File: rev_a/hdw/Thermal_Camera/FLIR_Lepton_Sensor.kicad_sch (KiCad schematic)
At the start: 25 parts

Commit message: lots of schematic progress
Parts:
- C?: renamed from C1102; footprint Capacitors_SMD:C_0603 -> (none); Digi-Key PN 1276-1935-1-ND -> (none); display_footprint 0603 -> (none)
- C? (x3): renamed from C1501; footprint Capacitors_SMD:C_0603 -> (none); Digi-Key PN 1276-1935-1-ND -> (none); display_footprint 0603 -> (none)
- C?: renamed from C1104; footprint Capacitors_SMD:C_0603 -> (none); Digi-Key PN 1276-1871-1-ND -> (none); display_footprint 0603 -> (none)
- L?: renamed from L1101; footprint Inductors_SMD:L_0603 -> (none); Digi-Key PN 490-1014-1-ND -> (none)
- R2401: renamed from R?; footprint Resistors_SMD:R_0603 -> (none); Digi-Key PN 541-10.0KHCT-ND -> (none); Wattage 1/10W -> (none); display_footprint 0603 -> (none)
- R2410, R2411, R2412, R2413, R2414: renamed from R?; footprint Resistors_SMD:R_0603 -> (none); Digi-Key PN 541-2982-1-ND -> (none); Wattage 1/10W -> (none); display_footprint 0603 -> (none)
- R?: renamed from R1103; footprint Resistors_SMD:R_0603 -> (none); Digi-Key PN 541-10.0HCT-ND -> (none); Wattage 1/10W -> (none); display_footprint 0603 -> (none)
- R? (x7): renamed from R1501; footprint Resistors_SMD:R_0603 -> (none); Digi-Key PN 541-10.0KHCT-ND -> (none); Wattage 1/10W -> (none); display_footprint 0603 -> (none)
- R?: renamed from R1105; footprint Resistors_SMD:R_0603 -> (none); Digi-Key PN 541-10.0KHCT-ND -> (none); Wattage 1/10W -> (none); display_footprint 0603 -> (none)
- gave numbers to parts that had none: 4

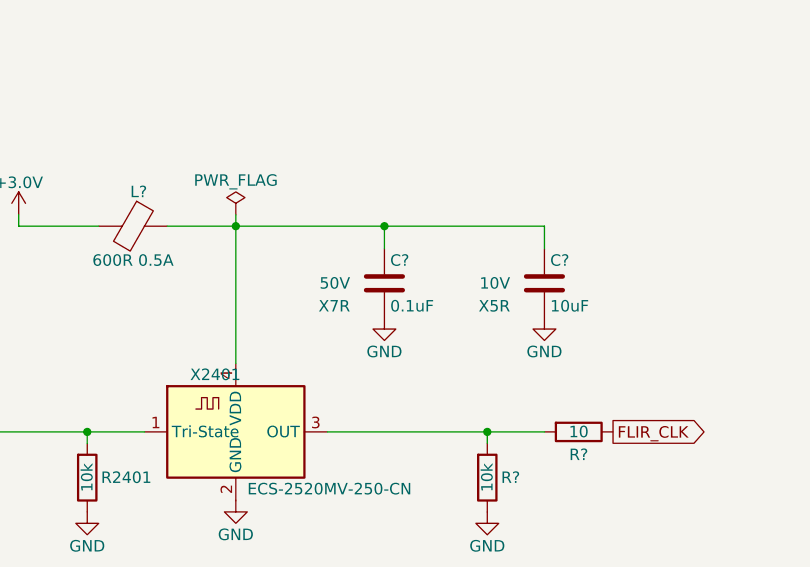
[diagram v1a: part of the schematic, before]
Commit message: assigned a ton of footprints
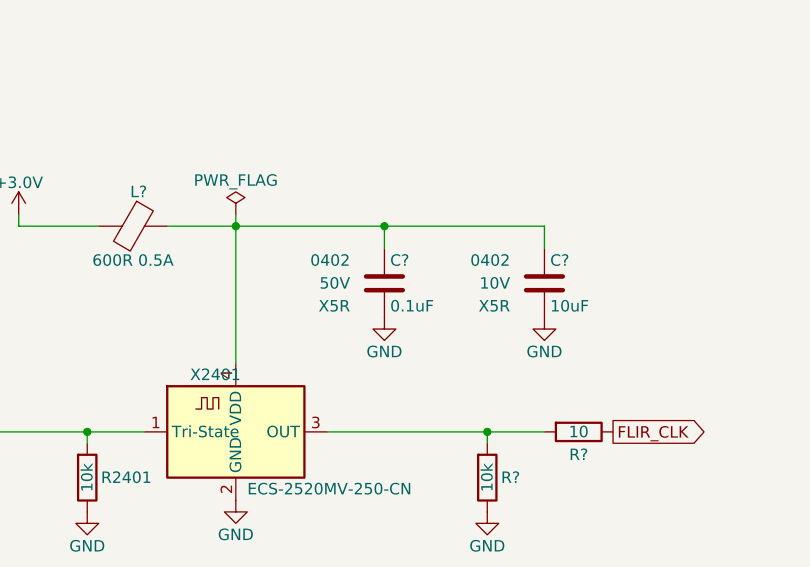
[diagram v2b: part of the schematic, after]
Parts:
- C? (x4): footprint (none) -> Capacitors_SMD:C_0402; Dielectric X7R -> X5R; display_footprint (none) -> 0402
- C?: footprint (none) -> Capacitors_SMD:C_0402; display_footprint (none) -> 0402
- L?: footprint (none) -> Inductors_SMD:L_0402
- R2401, R2410, R2411, R2412, R2413, R2414, R? (x9): footprint (none) -> Resistors_SMD:R_0402; Wattage (none) -> 1/16W; display_footprint (none) -> 0402
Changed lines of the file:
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@@
 			)
 		)
-		(property "Footprint" ""
+		(property "Footprint" "Resistors_SMD:R_0402"
 			(at 109.22 167.64 0)
 			(effects
@@
 			)
 		)
-		(property "display_footprint" ""
+		(property "display_footprint" "0402"
 			(at 109.22 165.1 90)
 			(effects
@@
 			)
 		)
-		(property "Wattage" ""
+		(property "Wattage" "1/16W"
 			(at 109.22 160.02 90)
 			(effects
@@
 			)
 		)
-		(property "Footprint" ""
+		(property "Footprint" "Resistors_SMD:R_0402"
 			(at 107.95 78.74 0)
 			(effects
@@
 			)
 		)
-		(property "display_footprint" ""
+		(property "display_footprint" "0402"
 			(at 110.236 76.2 0)
 			(effects
@@
 			)
 		)
-		(property "Wattage" ""
+		(property "Wattage" "1/16W"
 			(at 105.41 76.2 0)
 			(effects
@@
 			)
 		)
-		(property "Footprint" ""
+		(property "Footprint" "Capacitors_SMD:C_0402"
 			(at 88.5952 154.94 0)
 			(effects
@@
 			)
 		)
-		(property "display_footprint" ""
+		(property "display_footprint" "0402"
 			(at 83.82 148.59 0)
 			(effects
@@
 			)
 		)
-		(property "Dielectric" "X7R"
+		(property "Dielectric" "X5R"
 			(at 83.82 153.67 0)
 			(effects
@@
 			)
 		)
-		(property "Footprint" ""
+		(property "Footprint" "Resistors_SMD:R_0402"
 			(at 97.79 107.95 0)
 			(effects
@@
 			)
 		)
-		(property "display_footprint" ""
+		(property "display_footprint" "0402"
 			(at 100.33 106.172 0)
 			(effects
@@
 			)
 		)
-		(property "Wattage" ""
+		(property "Wattage" "1/16W"
 			(at 100.33 111.252 0)
 			(effects
@@
 			)
 		)
-		(property "Footprint" ""
+		(property "Footprint" "Inductors_SMD:L_0402"
 			(at 59.69 143.002 90)
 			(effects
@@
 			)
 		)
-		(property "Footprint" ""
+		(property "Footprint" "Resistors_SMD:R_0402"
 			(at 107.95 71.12 0)
 			(effects
@@
 			)
 		)
-		(property "display_footprint" ""
+		(property "display_footprint" "0402"
 			(at 110.236 68.58 0)
 			(effects
@@
 			)
 		)
-		(property "Wattage" ""
+		(property "Wattage" "1/16W"
 			(at 105.41 68.58 0)
 			(effects
@@
 			)
 		)
-		(property "Footprint" ""
+		(property "Footprint" "Resistors_SMD:R_0402"
 			(at 97.79 41.91 0)
 			(effects
@@
 			)
 		)
-		(property "display_footprint" ""
+		(property "display_footprint" "0402"
 			(at 100.33 40.132 0)
 			(effects
@@
 			)
 		)
-		(property "Wattage" ""
+		(property "Wattage" "1/16W"
 			(at 100.33 45.212 0)
 			(effects
@@
 			)
 		)
-		(property "Footprint" ""
+		(property "Footprint" "Resistors_SMD:R_0402"
 			(at 99.06 172.72 0)
 			(effects
@@
 			)
 		)
-		(property "display_footprint" ""
+		(property "display_footprint" "0402"
 			(at 97.282 170.688 0)
 			(effects
@@
 			)
 		)
-		(property "Wattage" ""
+		(property "Wattage" "1/16W"
 			(at 97.282 174.498 0)
 			(effects
@@
 			)
 		)
-		(property "Footprint" ""
+		(property "Footprint" "Resistors_SMD:R_0402"
 			(at 92.71 41.91 0)
 			(effects
@@
 			)
 		)
-		(property "display_footprint" ""
+		(property "display_footprint" "0402"
 			(at 95.25 40.132 0)
 			(effects
@@
 			)
 		)
-		(property "Wattage" ""
+		(property "Wattage" "1/16W"
 			(at 95.25 45.212 0)
 			(effects
@@
 			)
 		)
-		(property "Footprint" ""
+		(property "Footprint" "Resistors_SMD:R_0402"
 			(at 107.95 73.66 0)
 			(effects
@@
 			)
 		)
-		(property "display_footprint" ""
+		(property "display_footprint" "0402"
 			(at 110.236 71.12 0)
 			(effects
@@
 			)
 		)
-		(property "Wattage" ""
+		(property "Wattage" "1/16W"
 			(at 105.41 71.12 0)
 			(effects
@@
 			)
 		)
-		(property "Footprint" ""
+		(property "Footprint" "Resistors_SMD:R_0402"
 			(at 92.71 107.95 0)
 			(effects
@@
 			)
 		)
-		(property "display_footprint" ""
+		(property "display_footprint" "0402"
 			(at 95.25 106.172 0)
 			(effects
@@
 			)
 		)
-		(property "Wattage" ""
+		(property "Wattage" "1/16W"
 			(at 95.25 111.252 0)
 			(effects
@@
 			)
 		)
-		(property "Footprint" ""
+		(property "Footprint" "Resistors_SMD:R_0402"
 			(at 54.61 172.72 0)
 			(effects
@@
 			)
 		)
-		(property "display_footprint" ""
+		(property "display_footprint" "0402"
 			(at 52.832 170.688 0)
 			(effects
@@
 			)
 		)
-		(property "Wattage" ""
+		(property "Wattage" "1/16W"
 			(at 52.832 174.498 0)
 			(effects
@@
 			)
 		)
-		(property "Footprint" ""
+		(property "Footprint" "Capacitors_SMD:C_0402"
 			(at 120.9548 52.07 0)
 			(effects
@@
 			)
 		)
-		(property "display_footprint" ""
+		(property "display_footprint" "0402"
 			(at 125.73 45.72 0)
 			(effects
@@
 			)
 		)
-		(property "Dielectric" "X7R"
+		(property "Dielectric" "X5R"
 			(at 125.73 50.8 0)
 			(effects
@@
 			)
 		)
-		(property "Footprint" ""
+		(property "Footprint" "Resistors_SMD:R_0402"
 			(at 107.95 66.04 0)
 			(effects
@@
 			)
 		)
-		(property "display_footprint" ""
+		(property "display_footprint" "0402"
 			(at 110.236 63.5 0)
 			(effects
@@
 			)
 		)
-		(property "Wattage" ""
+		(property "Wattage" "1/16W"
 			(at 105.41 63.5 0)
 			(effects
@@
 			)
 		)
-		(property "Footprint" ""
+		(property "Footprint" "Resistors_SMD:R_0402"
 			(at 82.55 41.91 0)
 			(effects
@@
 			)
 		)
-		(property "display_footprint" ""
+		(property "display_footprint" "0402"
 			(at 85.09 40.132 0)
 			(effects
@@
 			)
 		)
-		(property "Wattage" ""
+		(property "Wattage" "1/16W"
 			(at 85.09 45.212 0)
 			(effects
@@
 			)
 		)
-		(property "Footprint" ""
+		(property "Footprint" "Resistors_SMD:R_0402"
 			(at 87.63 107.95 0)
 			(effects
@@
 			)
 		)
-		(property "display_footprint" ""
+		(property "display_footprint" "0402"
 			(at 90.17 106.172 0)
 			(effects
@@
 			)
 		)
-		(property "Wattage" ""
+		(property "Wattage" "1/16W"
 			(at 90.17 111.252 0)
 			(effects
@@
 			)
 		)
-		(property "Footprint" ""
+		(property "Footprint" "Resistors_SMD:R_0402"
 			(at 107.95 68.58 0)
 			(effects
@@
 			)
 		)
-		(property "display_footprint" ""
+		(property "display_footprint" "0402"
 			(at 110.236 66.04 0)
 			(effects
@@
 			)
 		)
-		(property "Wattage" ""
+		(property "Wattage" "1/16W"
 			(at 105.41 66.04 0)
 			(effects
@@
 			)
 		)
-		(property "Footprint" ""
+		(property "Footprint" "Capacitors_SMD:C_0402"
 			(at 108.2548 52.07 0)
 			(effects
@@
 			)
 		)
-		(property "display_footprint" ""
+		(property "display_footprint" "0402"
 			(at 113.03 45.72 0)
 			(effects
@@
 			)
 		)
-		(property "Dielectric" "X7R"
+		(property "Dielectric" "X5R"
 			(at 113.03 50.8 0)
 			(effects
@@
 			)
 		)
-		(property "Footprint" ""
+		(property "Footprint" "Capacitors_SMD:C_0402"
 			(at 106.3752 154.94 0)
 			(effects
@@
 			)
 		)
-		(property "display_footprint" ""
+		(property "display_footprint" "0402"
 			(at 101.6 148.59 0)
 			(effects
@@
 			)
 		)
-		(property "Footprint" ""
+		(property "Footprint" "Resistors_SMD:R_0402"
 			(at 87.63 41.91 0)
 			(effects
@@
 			)
 		)
-		(property "display_footprint" ""
+		(property "display_footprint" "0402"
 			(at 90.17 40.132 0)
 			(effects
@@
 			)
 		)
-		(property "Wattage" ""
+		(property "Wattage" "1/16W"
 			(at 90.17 45.212 0)
 			(effects
@@
 			)
 		)
-		(property "Footprint" ""
+		(property "Footprint" "Capacitors_SMD:C_0402"
 			(at 133.6548 52.07 0)
 			(effects
@@
 			)
 		)
-		(property "display_footprint" ""
+		(property "display_footprint" "0402"
 			(at 138.43 45.72 0)
 			(effects
@@
 			)
 		)
-		(property "Dielectric" "X7R"
+		(property "Dielectric" "X5R"
 			(at 138.43 50.8 0)
 			(effects

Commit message: assigned some part numbers
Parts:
- C? (x4): Digi-Key PN (none) -> 490-10697-1-ND
- C?: Digi-Key PN (none) -> 490-GRM155R61A106ME11DCT-ND
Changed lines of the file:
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@@
 			)
 		)
-		(property "Digi-Key PN" ""
+		(property "Digi-Key PN" "490-10697-1-ND"
 			(at -11.684 325.882 0)
 			(effects
@@
 			)
 		)
-		(property "Digi-Key PN" ""
+		(property "Digi-Key PN" "490-10697-1-ND"
 			(at 111.125 35.56 0)
 			(effects
@@
 			)
 		)
-		(property "Digi-Key PN" ""
+		(property "Digi-Key PN" "490-10697-1-ND"
 			(at 98.425 35.56 0)
 			(effects
@@
 			)
 		)
-		(property "Digi-Key PN" ""
+		(property "Digi-Key PN" "490-GRM155R61A106ME11DCT-ND"
 			(at 105.41 151.13 0)
 			(effects
@@
 			)
 		)
-		(property "Digi-Key PN" ""
+		(property "Digi-Key PN" "490-10697-1-ND"
 			(at 123.825 35.56 0)
 			(effects

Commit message: assigned resistor part numbers
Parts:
- R2401, R? (x8): Digi-Key PN (none) -> RMCF0402FT10K0CT-ND
- R2410, R2411, R2412, R2413, R2414, R?: Digi-Key PN (none) -> RMCF0402FT10R0CT-ND
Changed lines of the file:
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@@
 			)
 		)
-		(property "Digi-Key PN" ""
+		(property "Digi-Key PN" "RMCF0402FT10R0CT-ND"
 			(at 99.06 160.02 0)
 			(effects
@@
 			)
 		)
-		(property "Digi-Key PN" ""
+		(property "Digi-Key PN" "RMCF0402FT10R0CT-ND"
 			(at 107.95 78.74 0)
 			(effects
@@
 			)
 		)
-		(property "Digi-Key PN" ""
+		(property "Digi-Key PN" "RMCF0402FT10K0CT-ND"
 			(at 105.41 97.79 0)
 			(effects
@@
 			)
 		)
-		(property "Digi-Key PN" ""
+		(property "Digi-Key PN" "RMCF0402FT10R0CT-ND"
 			(at 107.95 71.12 0)
 			(effects
@@
 			)
 		)
-		(property "Digi-Key PN" ""
+		(property "Digi-Key PN" "RMCF0402FT10K0CT-ND"
 			(at 105.41 31.75 0)
 			(effects
@@
 			)
 		)
-		(property "Digi-Key PN" ""
+		(property "Digi-Key PN" "RMCF0402FT10K0CT-ND"
 			(at 99.06 172.72 0)
 			(effects
@@
 			)
 		)
-		(property "Digi-Key PN" ""
+		(property "Digi-Key PN" "RMCF0402FT10K0CT-ND"
 			(at 100.33 31.75 0)
 			(effects
@@
 			)
 		)
-		(property "Digi-Key PN" ""
+		(property "Digi-Key PN" "RMCF0402FT10R0CT-ND"
 			(at 107.95 73.66 0)
 			(effects
@@
 			)
 		)
-		(property "Digi-Key PN" ""
+		(property "Digi-Key PN" "RMCF0402FT10K0CT-ND"
 			(at 100.33 97.79 0)
 			(effects
@@
 			)
 		)
-		(property "Digi-Key PN" ""
+		(property "Digi-Key PN" "RMCF0402FT10K0CT-ND"
 			(at 54.61 172.72 0)
 			(effects
@@
 			)
 		)
-		(property "Digi-Key PN" ""
+		(property "Digi-Key PN" "RMCF0402FT10R0CT-ND"
 			(at 107.95 66.04 0)
 			(effects
@@
 			)
 		)
-		(property "Digi-Key PN" ""
+		(property "Digi-Key PN" "RMCF0402FT10K0CT-ND"
 			(at 90.17 31.75 0)
 			(effects
@@
 			)
 		)
-		(property "Digi-Key PN" ""
+		(property "Digi-Key PN" "RMCF0402FT10K0CT-ND"
 			(at 95.25 97.79 0)
 			(effects
@@
 			)
 		)
-		(property "Digi-Key PN" ""
+		(property "Digi-Key PN" "RMCF0402FT10R0CT-ND"
 			(at 107.95 68.58 0)
 			(effects
@@
 			)
 		)
-		(property "Digi-Key PN" ""
+		(property "Digi-Key PN" "RMCF0402FT10K0CT-ND"
 			(at 95.25 31.75 0)
 			(effects
